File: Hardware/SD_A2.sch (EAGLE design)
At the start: 30 parts, among them IC1 74HCT245N, IC2 LM317, IC3 2716 / 2732, IC4 XC9572XL

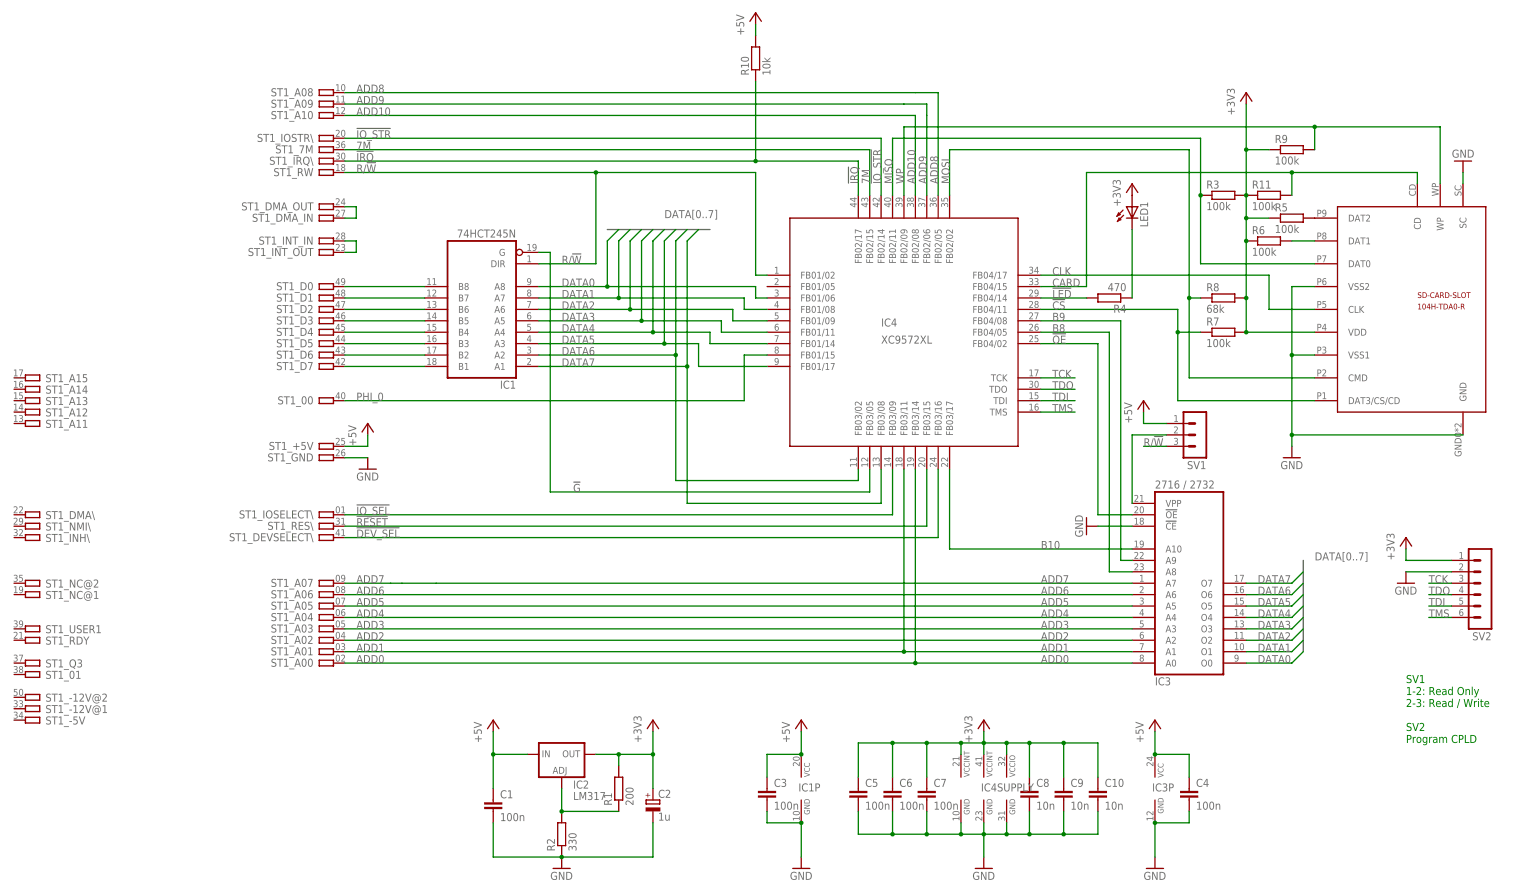
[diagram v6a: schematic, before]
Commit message: IRQ Pin removed, A11 added
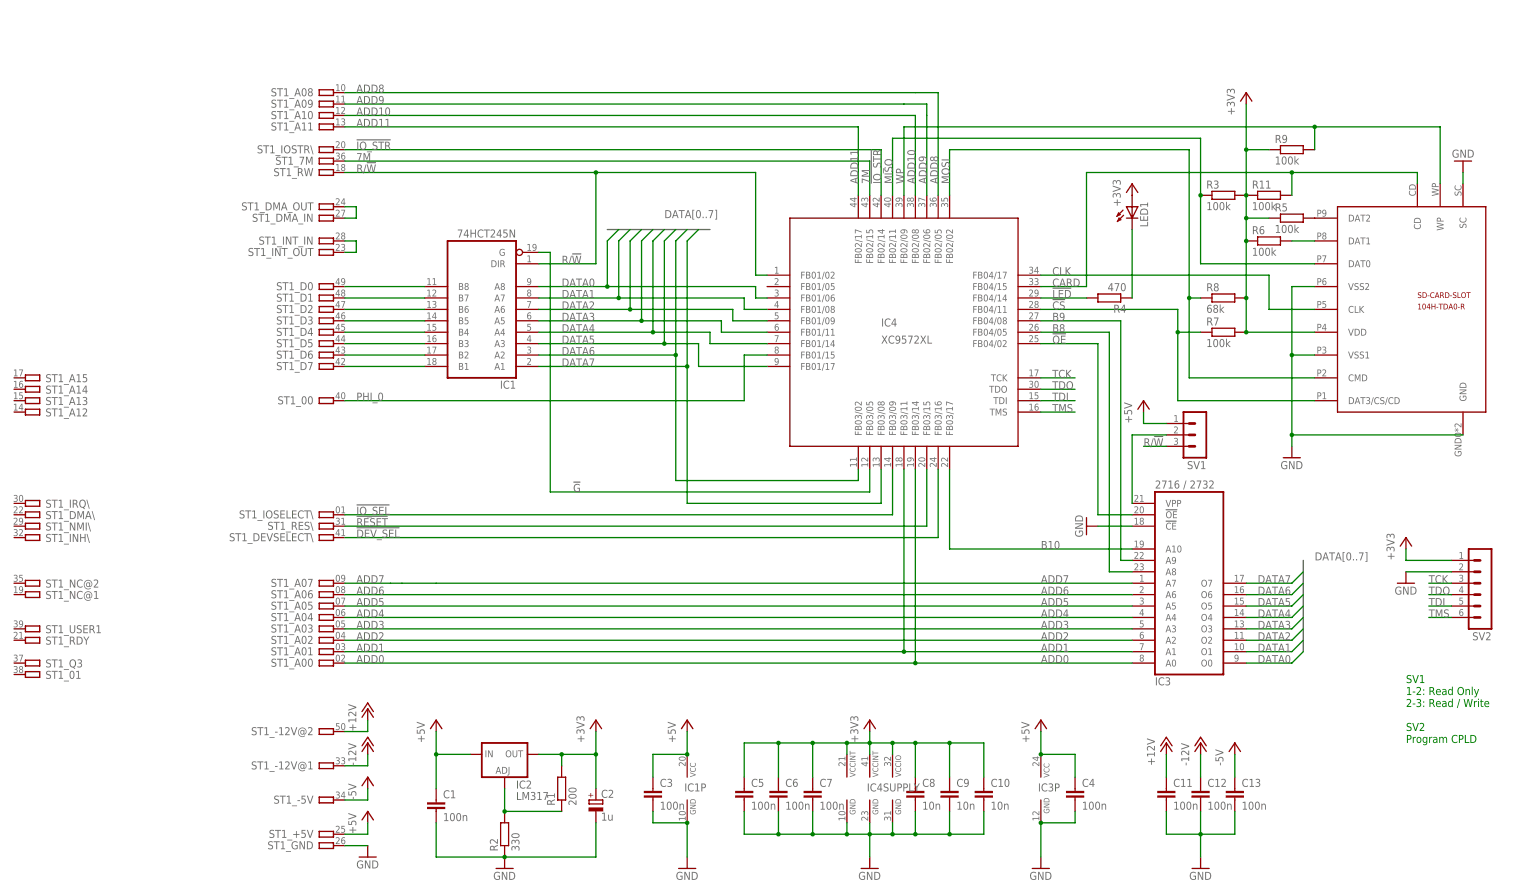
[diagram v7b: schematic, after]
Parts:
- removed R10: 10k, rcl:R-EU_R0603
- added C11, C12, C13: 100n, rcl:C-EUC0603K
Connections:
- removed net !IRQ: IC4G$1.FB02/17, R10.1, ST1_IRQ\.P
- new net +12V: C11.1, ST1_-12V@2.P
- new net -12V: C12.1, ST1_-12V@1.P
- new net -5V: C13.1, ST1_-5V.P
- new net ADD11: IC4G$1.FB02/17, ST1_A11.P
- net +5V: no longer R10.2
- net GND: now also C11.2, C12.2, C13.2
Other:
- moved on the sheet: C1, C10, C2, C3, C4, C5, C6, C7, C8, C9, IC1P, IC2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

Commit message: Schematic updated
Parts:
- IC1: value 74HCT245N -> 74LS245N; device 74xx-eu:74HCT245N -> 74xx-eu:74LS245N
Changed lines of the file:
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@@
 <part name="ST1" library="con-apple2" deviceset="A2-50PIN" device="SLOT1-3"/>
 <part name="IC4" library="xilinx-xc9" deviceset="XC9572_S44" device="" value="XC9572XL"/>
-<part name="IC1" library="74xx-eu" deviceset="74*245" device="N" technology="HCT"/>
+<part name="IC1" library="74xx-eu" library_urn="urn:adsk.eagle:library:85" deviceset="74*245" device="N" technology="LS" value="74LS245N"/>
 <part name="IC2" library="v-reg" deviceset="LM317TL" device="" value="LM317"/>
 <part name="C2" library="rcl" library_urn="urn:adsk.eagle:library:334" deviceset="CPOL-EU" device="153CLV-0405" value="1u"/>
